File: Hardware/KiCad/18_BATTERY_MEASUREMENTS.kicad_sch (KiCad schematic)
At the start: 0 parts

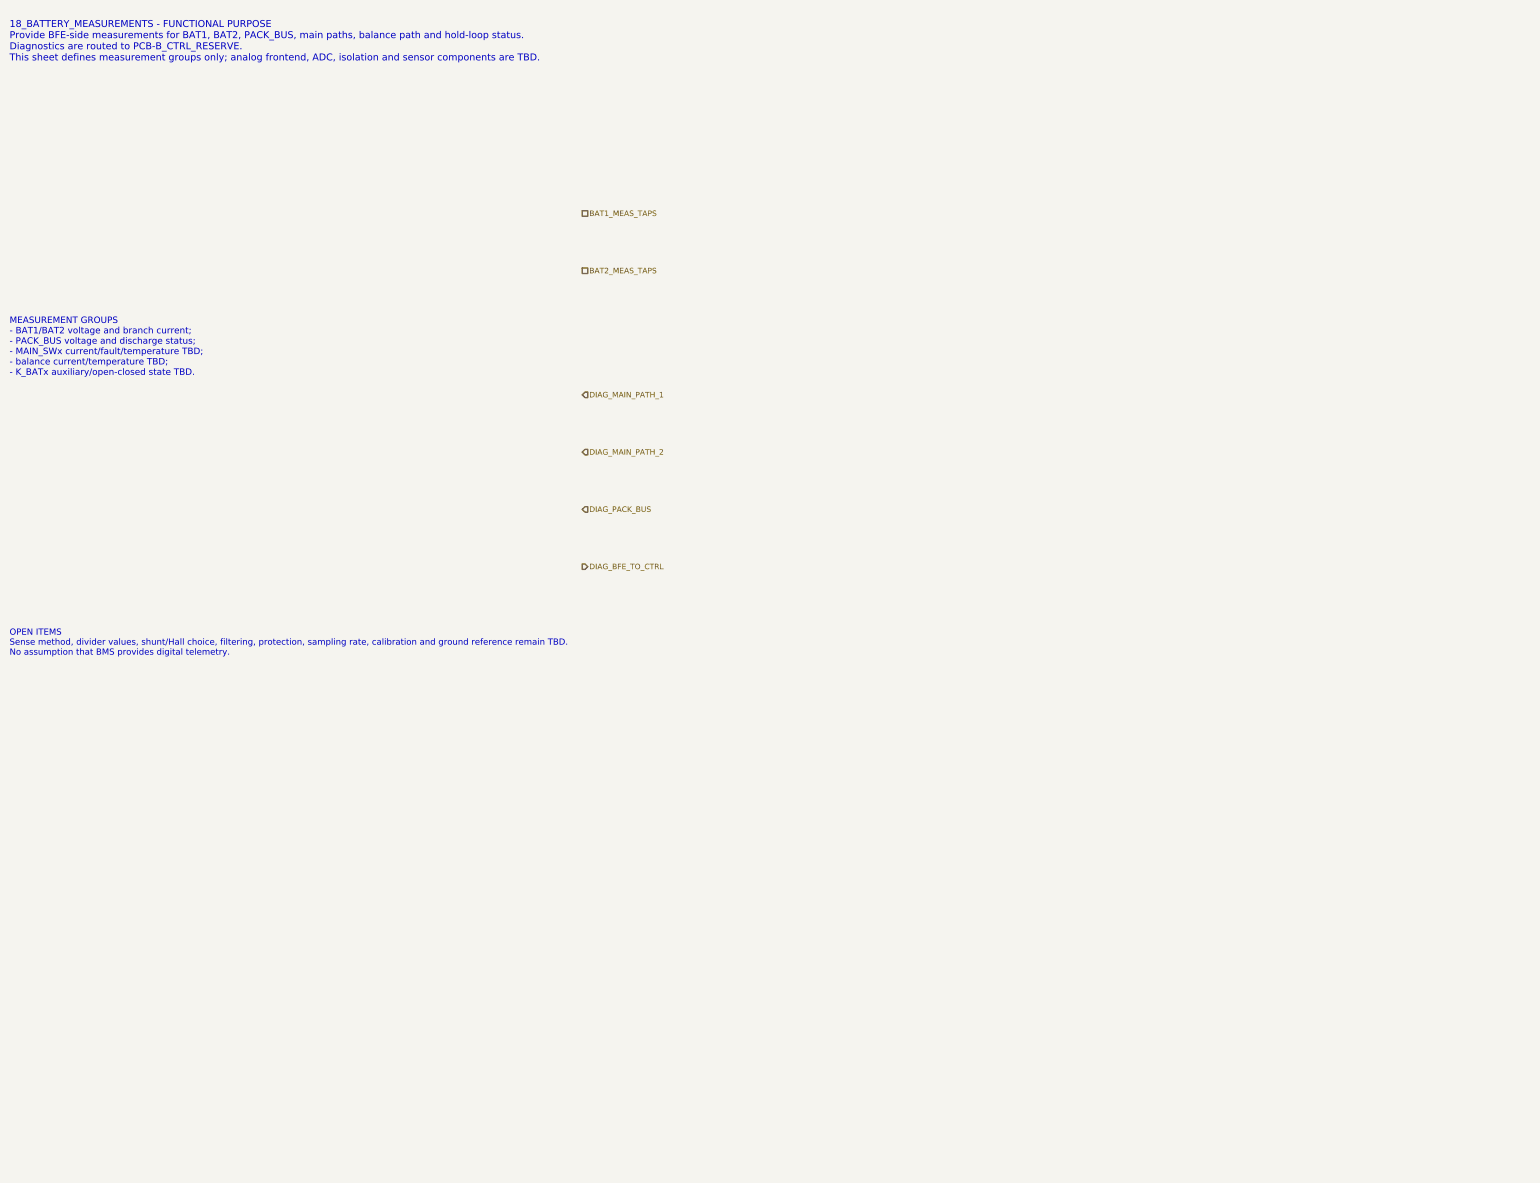
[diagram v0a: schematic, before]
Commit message: hardware: refine BFE measurements level B
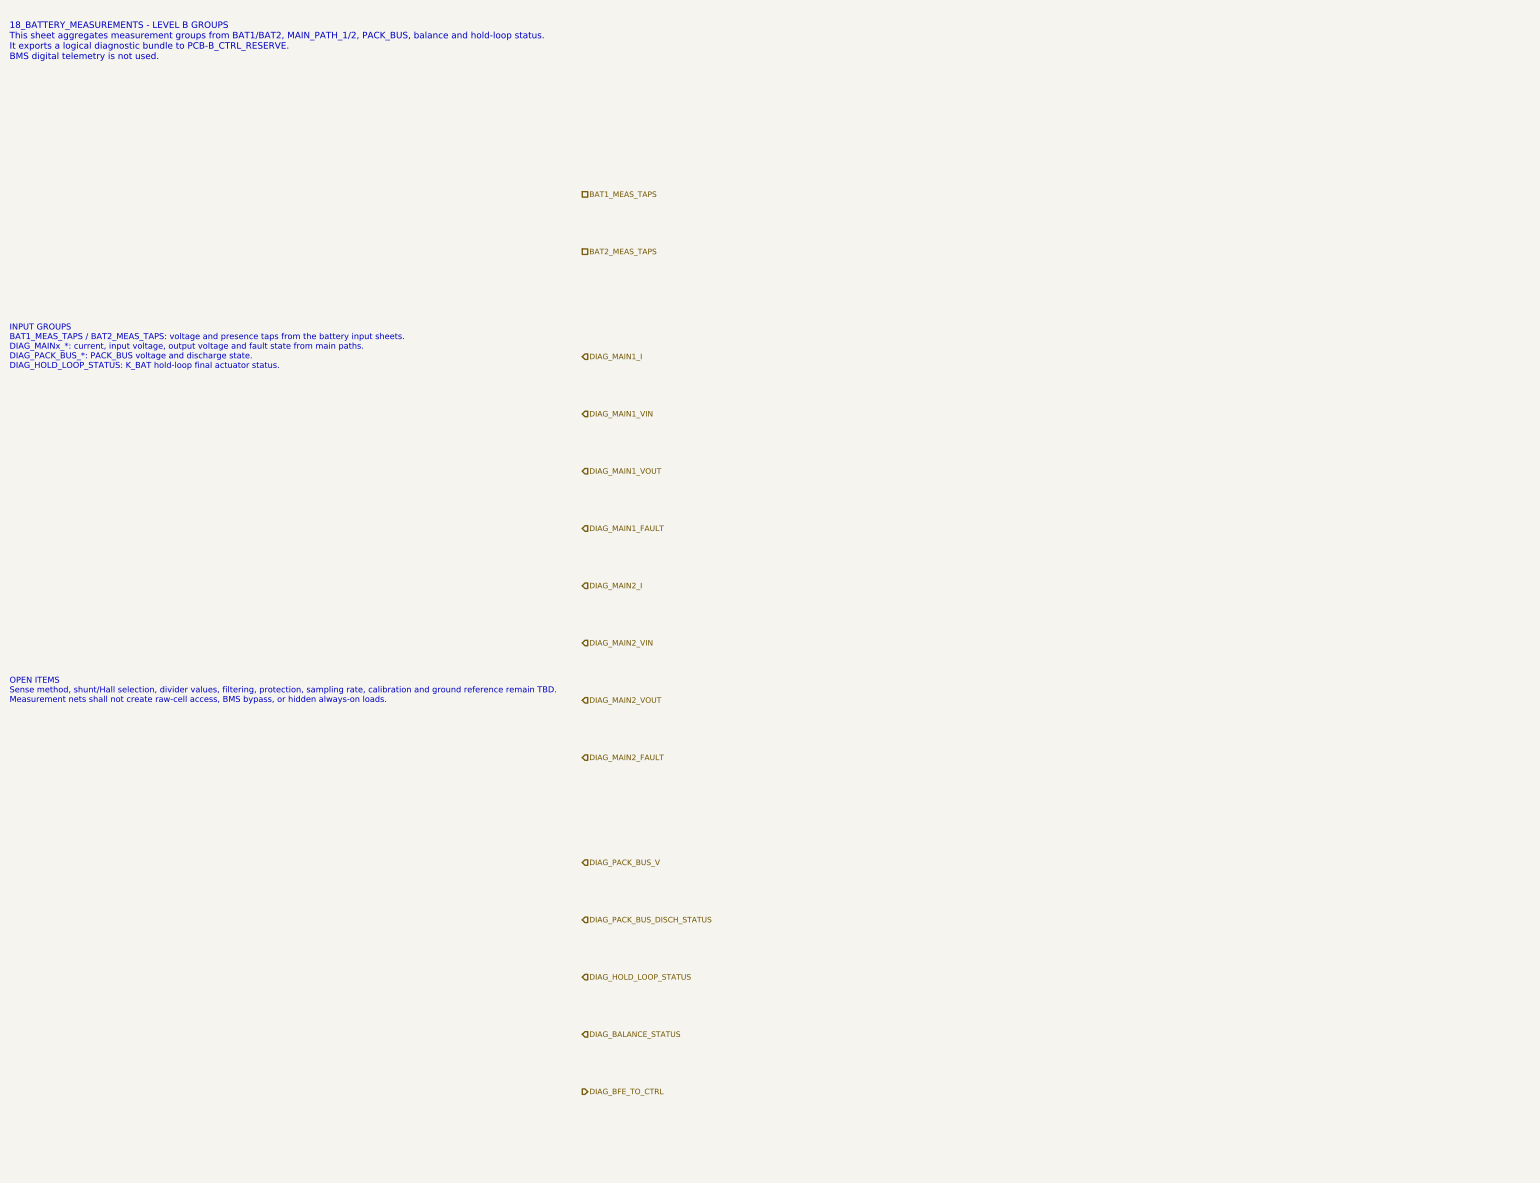
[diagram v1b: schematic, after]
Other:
- note added: "18_BATTERY_MEASUREMENTS - LEVEL B GROUPS This sheet aggregates measurement groups from BAT1/BAT2, MAIN_PATH_1/2, PACK_BUS, balance and hold-loop status. It exports a logical diagnostic bundle to PCB-B_CTRL_RESERVE. BMS digital telemetry is not used."
- note added: "INPUT GROUPS BAT1_MEAS_TAPS / BAT2_MEAS_TAPS: voltage and presence taps from the battery input sheets. DIAG_MAINx_*: current, input voltage, output voltage and fault state from main paths. DIAG_PACK_BUS_*: PACK_BUS voltage and discharge state. DIAG_HOLD_LOOP_STATUS: K_BAT hold-loop final actuator status."
- note added: "OPEN ITEMS Sense method, shunt/Hall selection, divider values, filtering, protection, sampling rate, calibration and ground reference remain TBD. Measurement nets shall not create raw-cell access, BMS bypass, or hidden always-on loads."
- note removed: "18_BATTERY_MEASUREMENTS - FUNCTIONAL PURPOSE Provide BFE-side measurements for BAT1, BAT2, PACK_BUS, main paths, balance path and hold-loop status. Diagnostics are routed to PCB-B_CTRL_RESERVE. This sheet defines measurement groups only; analog frontend, ADC, isolation and sensor components are TBD."
- note removed: "MEASUREMENT GROUPS - BAT1/BAT2 voltage and branch current; - PACK_BUS voltage and discharge status; - MAIN_SWx current/fault/temperature TBD; - balance current/temperature TBD; - K_BATx auxiliary/open-closed state TBD."
- note removed: "OPEN ITEMS Sense method, divider values, shunt/Hall choice, filtering, protection, sampling rate, calibration and ground reference remain TBD. No assumption that BMS provides digital telemetry."
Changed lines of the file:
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@@
 	(generator "eeschema")
 	(generator_version "10.0")
-	(uuid "bfe-dh-00000018-0000-4000-8000-000000000018")
+	(uuid "bfe-lb-00000018-0000-4000-8000-000000000018")
 	(paper "A3")
 	(title_block
 		(title "18_BATTERY_MEASUREMENTS - BFE sensing boundary")
 		(date "2026-07-15")
-		(rev "A1")
+		(rev "B1")
 		(company "Gonoboben/plataVM")
-		(comment 1 "Architecture Level A: voltage/current/status sensing boundary")
-		(comment 2 "No ADC frontend, current sensor or isolation topology selected")
+		(comment 1 "Architecture Level B: measurement group names and diagnostic aggregation")
+		(comment 2 "No ADC frontend, current sensor, divider values or isolation topology selected")
 	)
-	(text "18_BATTERY_MEASUREMENTS - FUNCTIONAL PURPOSE\nProvide BFE-side measurements for BAT1, BAT2, PACK_BUS, main paths, balance path and hold-loop status.\nDiagnostics are routed to PCB-B_CTRL_RESERVE.\nThis sheet defines measurement groups only; analog frontend, ADC, isolation and sensor components are TBD."
+	(text "18_BATTERY_MEASUREMENTS - LEVEL B GROUPS\nThis sheet aggregates measurement groups from BAT1/BAT2, MAIN_PATH_1/2, PACK_BUS, balance and hold-loop status.\nIt exports a logical diagnostic bundle to PCB-B_CTRL_RESERVE.\nBMS digital telemetry is not used."
 		(exclude_from_sim no)
 		(at 12 18 0)
-		(effects (font (size 1.45 1.45)) (justify left))
-		(uuid "bfe-dh-00000018-0000-4000-8000-000000000101")
+		(effects (font (size 1.35 1.35)) (justify left))
+		(uuid "bfe-lb-00000018-0000-4000-8000-000000000101")
 	)
-	(text "MEASUREMENT GROUPS\n- BAT1/BAT2 voltage and branch current;\n- PACK_BUS voltage and discharge status;\n- MAIN_SWx current/fault/temperature TBD;\n- balance current/temperature TBD;\n- K_BATx auxiliary/open-closed state TBD."
+	(text "INPUT GROUPS\nBAT1_MEAS_TAPS / BAT2_MEAS_TAPS: voltage and presence taps from the battery input sheets.\nDIAG_MAINx_*: current, input voltage, output voltage and fault state from main paths.\nDIAG_PACK_BUS_*: PACK_BUS voltage and discharge state.\nDIAG_HOLD_LOOP_STATUS: K_BAT hold-loop final actuator status."
 		(exclude_from_sim no)
 		(at 12 82 0)
-		(effects (font (size 1.35 1.35)) (justify left))
-		(uuid "bfe-dh-00000018-0000-4000-8000-000000000102")
+		(effects (font (size 1.25 1.25)) (justify left))
+		(uuid "bfe-lb-00000018-0000-4000-8000-000000000102")
 	)
-	(text "OPEN ITEMS\nSense method, divider values, shunt/Hall choice, filtering, protection, sampling rate, calibration and ground reference remain TBD.\nNo assumption that BMS provides digital telemetry."
+	(text "OPEN ITEMS\nSense method, shunt/Hall selection, divider values, filtering, protection, sampling rate, calibration and ground reference remain TBD.\nMeasurement nets shall not create raw-cell access, BMS bypass, or hidden always-on loads."
 		(exclude_from_sim no)
-		(at 12 144 0)
-		(effects (font (size 1.3 1.3)) (justify left))
-		(uuid "bfe-dh-00000018-0000-4000-8000-000000000103")
+		(at 12 154 0)
+		(effects (font (size 1.25 1.25)) (justify left))
+		(uuid "bfe-lb-00000018-0000-4000-8000-000000000103")
 	)
-	(hierarchical_label "BAT1_MEAS_TAPS" (shape passive) (exclude_from_sim no) (at 132 54 0) (effects (font (size 1.15 1.15)) (justify left)) (uuid "bfe-dh-00000018-0000-4000-8000-000000000201"))
-	(hierarchical_label "BAT2_MEAS_TAPS" (shape passive) (exclude_from_sim no) (at 132 66 0) (effects (font (size 1.15 1.15)) (justify left)) (uuid "bfe-dh-00000018-0000-4000-8000-000000000202"))
-	(hierarchical_label "DIAG_MAIN_PATH_1" (shape input) (exclude_from_sim no) (at 132 92 0) (effects (font (size 1.15 1.15)) (justify left)) (uuid "bfe-dh-00000018-0000-4000-8000-000000000203"))
-	(hierarchical_label "DIAG_MAIN_PATH_2" (shape input) (exclude_from_sim no) (at 132 104 0) (effects (font (size 1.15 1.15)) (justify left)) (uuid "bfe-dh-00000018-0000-4000-8000-000000000204"))
-	(hierarchical_label "DIAG_PACK_BUS" (shape input) (exclude_from_sim no) (at 132 116 0) (effects (font (size 1.15 1.15)) (justify left)) (uuid "bfe-dh-00000018-0000-4000-8000-000000000205"))
-	(hierarchical_label "DIAG_BFE_TO_CTRL" (shape output) (exclude_from_sim no) (at 132 128 0) (effects (font (size 1.15 1.15)) (justify left)) (uuid "bfe-dh-00000018-0000-4000-8000-000000000206"))
+	(hierarchical_label "BAT1_MEAS_TAPS" (shape passive) (exclude_from_sim no) (at 132 50 0) (effects (font (size 1.15 1.15)) (justify left)) (uuid "bfe-lb-00000018-0000-4000-8000-000000000201"))
+	(hierarchical_label "BAT2_MEAS_TAPS" (shape passive) (exclude_from_sim no) (at 132 62 0) (effects (font (size 1.15 1.15)) (justify left)) (uuid "bfe-lb-00000018-0000-4000-8000-000000000202"))
+	(hierarchical_label "DIAG_MAIN1_I" (shape input) (exclude_from_sim no) (at 132 84 0) (effects (font (size 1.15 1.15)) (justify left)) (uuid "bfe-lb-00000018-0000-4000-8000-000000000203"))
+	(hierarchical_label "DIAG_MAIN1_VIN" (shape input) (exclude_from_sim no) (at 132 96 0) (effects (font (size 1.15 1.15)) (justify left)) (uuid "bfe-lb-00000018-0000-4000-8000-000000000204"))
+	(hierarchical_label "DIAG_MAIN1_VOUT" (shape input) (exclude_from_sim no) (at 132 108 0) (effects (font (size 1.15 1.15)) (justify left)) (uuid "bfe-lb-00000018-0000-4000-8000-000000000205"))
+	(hierarchical_label "DIAG_MAIN1_FAULT" (shape input) (exclude_from_sim no) (at 132 120 0) (effects (font (size 1.15 1.15)) (justify left)) (uuid "bfe-lb-00000018-0000-4000-8000-000000000206"))
+	(hierarchical_label "DIAG_MAIN2_I" (shape input) (exclude_from_sim no) (at 132 132 0) (effects (font (size 1.15 1.15)) (justify left)) (uuid "bfe-lb-00000018-0000-4000-8000-000000000207"))
+	(hierarchical_label "DIAG_MAIN2_VIN" (shape input) (exclude_from_sim no) (at 132 144 0) (effects (font (size 1.15 1.15)) (justify left)) (uuid "bfe-lb-00000018-0000-4000-8000-000000000208"))
+	(hierarchical_label "DIAG_MAIN2_VOUT" (shape input) (exclude_from_sim no) (at 132 156 0) (effects (font (size 1.15 1.15)) (justify left)) (uuid "bfe-lb-00000018-0000-4000-8000-000000000209"))
+	(hierarchical_label "DIAG_MAIN2_FAULT" (shape input) (exclude_from_sim no) (at 132 168 0) (effects (font (size 1.15 1.15)) (justify left)) (uuid "bfe-lb-00000018-0000-4000-8000-000000000210"))
+	(hierarchical_label "DIAG_PACK_BUS_V" (shape input) (exclude_from_sim no) (at 132 190 0) (effects (font (size 1.15 1.15)) (justify left)) (uuid "bfe-lb-00000018-0000-4000-8000-000000000211"))
+	(hierarchical_label "DIAG_PACK_BUS_DISCH_STATUS" (shape input) (exclude_from_sim no) (at 132 202 0) (effects (font (size 1.15 1.15)) (justify left)) (uuid "bfe-lb-00000018-0000-4000-8000-000000000212"))
+	(hierarchical_label "DIAG_HOLD_LOOP_STATUS" (shape input) (exclude_from_sim no) (at 132 214 0) (effects (font (size 1.15 1.15)) (justify left)) (uuid "bfe-lb-00000018-0000-4000-8000-000000000213"))
+	(hierarchical_label "DIAG_BALANCE_STATUS" (shape input) (exclude_from_sim no) (at 132 226 0) (effects (font (size 1.15 1.15)) (justify left)) (uuid "bfe-lb-00000018-0000-4000-8000-000000000214"))
+	(hierarchical_label "DIAG_BFE_TO_CTRL" (shape output) (exclude_from_sim no) (at 132 238 0) (effects (font (size 1.15 1.15)) (justify left)) (uuid "bfe-lb-00000018-0000-4000-8000-000000000215"))
 )
